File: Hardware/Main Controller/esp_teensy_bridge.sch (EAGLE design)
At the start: 55 parts, among them IC1 BQ79600PWRQ1, Q1 SI7611DN-T1-GE3, Q2 SI7611DN-T1-GE3, Q3 SI7611DN-T1-GE3

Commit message: fixed some inconsistencies
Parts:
- removed CCB1, CCB22, CCB23, CCB4: 220 pF, capacitor-wima:C2.5/2
- removed CCB2, CCB24, CCB25, CCB3: 2.2nf, capacitor-wima:C2.5/2
- removed COMH, COML: 5566-2, con-molex:5566-2
- removed RVC1, RVC17: 1k, rcl:R-US_R0603
- removed RVC18, RVC19, RVC2, RVC3: 49, rcl:R-US_R0603
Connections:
- removed net N$6: CCB3.2, RVC3.1
- removed net N$66: CCB25.1, COMH-2.S
- removed net N$67: CCB25.2, RVC19.1
- removed net N$68: CCB24.2, RVC18.1
- removed net N$69: CCB24.1, COMH-1.S
- removed net N$7: CCB2.2, RVC2.1
- removed net N$8: CCB2.1, COML-1.S
- removed net N$9: CCB3.1, COML-2.S
- net COMHN: no longer CCB22.2, RVC17.1, RVC18.2
- net COMHP: no longer CCB23.2, RVC17.2, RVC19.2
- net COMLN: no longer CCB4.2, RVC1.2, RVC3.2
- net COMLP: no longer CCB1.2, RVC1.1, RVC2.2
- net GND: no longer CCB1.1, CCB22.1, CCB23.1, CCB4.1
- net VCC: now also CONTACTOR_N-1.S, CONTACTOR_P-1.S, CONTACTOR_PRECHARGE-1.S

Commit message: 12/1/2021
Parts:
- added COOLANT-1: 5566-2, con-molex:5566-2
- added Q4: SI7611DN-T1-GE3, SI7611DN-T1-GE3:SI7611DN-T1-GE3
- added R1: 10k, rcl:R-US_R0603
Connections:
- new net COOLANT_CTRL: Q4.G, R1.2
- new net N$6: COOLANT-1-2.S, Q4.S
- net GND: now also Q4.D, R1.1
- net VCC: now also COOLANT-1-1.S
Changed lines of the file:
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@@
 <part name="R7" library="rcl" library_urn="urn:adsk.eagle:library:334" deviceset="R-US_" device="R0603" package3d_urn="urn:adsk.eagle:package:23555/3" value="10k"/>
 <part name="R8" library="rcl" library_urn="urn:adsk.eagle:library:334" deviceset="R-US_" device="R0603" package3d_urn="urn:adsk.eagle:package:23555/3" value="100k"/>
+<part name="COOLANT-1" library="con-molex" library_urn="urn:adsk.eagle:library:165" deviceset="5566-2" device="" package3d_urn="urn:adsk.eagle:package:8078583/1"/>
+<part name="Q4" library="SI7611DN-T1-GE3" deviceset="SI7611DN-T1-GE3" device=""/>
+<part name="R1" library="rcl" library_urn="urn:adsk.eagle:library:334" deviceset="R-US_" device="R0603" package3d_urn="urn:adsk.eagle:package:23555/3" value="10k"/>
 </parts>
 <sheets>
@@
 <attribute name="NAME" x="-13.97" y="67.5386" size="1.778" layer="95"/>
 <attribute name="VALUE" x="-13.97" y="62.738" size="1.778" layer="96"/>
+</instance>
+<instance part="COOLANT-1" gate="-1" x="-119.38" y="12.7" smashed="yes">
+<attribute name="NAME" x="-116.84" y="11.938" size="1.524" layer="95"/>
+<attribute name="VALUE" x="-120.142" y="14.097" size="1.778" layer="96"/>
+</instance>
+<instance part="COOLANT-1" gate="-2" x="-119.38" y="7.62" smashed="yes">
+<attribute name="NAME" x="-116.84" y="6.858" size="1.524" layer="95"/>
+<attribute name="VALUE" x="-120.142" y="9.017" size="1.778" layer="96"/>
+</instance>
+<instance part="Q4" gate="G$1" x="-132.08" y="10.16" smashed="yes">
+<attribute name="VALUE" x="-140.97796875" y="3.804309375" size="1.779590625" layer="96"/>
+<attribute name="NAME" x="-140.987490625" y="13.977490625" size="1.7815" layer="95"/>
+</instance>
+<instance part="R1" gate="G$1" x="-139.7" y="17.78" smashed="yes">
+<attribute name="NAME" x="-143.51" y="19.2786" size="1.778" layer="95"/>
+<attribute name="VALUE" x="-143.51" y="14.478" size="1.778" layer="96"/>
 </instance>
 </instances>
@@
 <label x="-15.24" y="-50.8" size="1.778" layer="95"/>
 </segment>
+<segment>
+<pinref part="Q4" gate="G$1" pin="D"/>
+<wire x1="-129.54" y1="5.08" x2="-129.54" y2="2.54" width="0.1524" layer="91"/>
+<label x="-129.54" y="0" size="1.778" layer="95"/>
+<wire x1="-144.78" y1="17.78" x2="-144.78" y2="2.54" width="0.1524" layer="91"/>
+<wire x1="-144.78" y1="2.54" x2="-129.54" y2="2.54" width="0.1524" layer="91"/>
+<pinref part="R1" gate="G$1" pin="1"/>
+</segment>
 </net>
 <net name="NCS/CS" class="0">
@@
 <wire x1="-121.92" y1="35.56" x2="-124.46" y2="35.56" width="0.1524" layer="91"/>
 <label x="-124.46" y="35.56" size="1.778" layer="95"/>
+</segment>
+<segment>
+<pinref part="COOLANT-1" gate="-1" pin="S"/>
+<wire x1="-121.92" y1="12.7" x2="-124.46" y2="12.7" width="0.1524" layer="91"/>
+<label x="-124.46" y="12.7" size="1.778" layer="95"/>
 </segment>
 </net>
@@
 </segment>
 </net>
+<net name="N$6" class="0">
+<segment>
+<pinref part="Q4" gate="G$1" pin="S"/>
+<wire x1="-129.54" y1="15.24" x2="-127" y2="15.24" width="0.1524" layer="91"/>
+<wire x1="-127" y1="15.24" x2="-127" y2="7.62" width="0.1524" layer="91"/>
+<pinref part="COOLANT-1" gate="-2" pin="S"/>
+<wire x1="-127" y1="7.62" x2="-121.92" y2="7.62" width="0.1524" layer="91"/>
+</segment>
+</net>
+<net name="COOLANT_CTRL" class="0">
+<segment>
+<pinref part="Q4" gate="G$1" pin="G"/>
+<wire x1="-134.62" y1="17.78" x2="-134.62" y2="12.7" width="0.1524" layer="91"/>
+<label x="-132.08" y="17.78" size="1.778" layer="95"/>
+<pinref part="R1" gate="G$1" pin="2"/>
+</segment>
+</net>

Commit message: have fun with eagle
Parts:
- C1, C2, C4, C5: device capacitor-wima:C2,5-3 -> rcl:C-EUC0603
- C3: device capacitor-wima:C2.5/2 -> rcl:C-EUC0603
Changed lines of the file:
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@@
 <part name="IC1" library="BQ79600" deviceset="BQ79600PWRQ1" device=""/>
 <part name="U$2" library="ESP32-DEVKITV1" deviceset="ESP32DEVKITV1" device=""/>
-<part name="C1" library="capacitor-wima" library_urn="urn:adsk.eagle:library:116" deviceset="C" device="2,5-3" package3d_urn="urn:adsk.eagle:package:5436/1" value="0.22μF"/>
-<part name="C2" library="capacitor-wima" library_urn="urn:adsk.eagle:library:116" deviceset="C" device="2,5-3" package3d_urn="urn:adsk.eagle:package:5436/1" value="0.1μF"/>
-<part name="C3" library="capacitor-wima" library_urn="urn:adsk.eagle:library:116" deviceset="C" device="2.5/2" package3d_urn="urn:adsk.eagle:package:5415/1" value="0.22uF"/>
+<part name="C1" library="rcl" library_urn="urn:adsk.eagle:library:334" deviceset="C-EU" device="C0603" package3d_urn="urn:adsk.eagle:package:23616/2" value="0.22μF"/>
+<part name="C2" library="rcl" library_urn="urn:adsk.eagle:library:334" deviceset="C-EU" device="C0603" package3d_urn="urn:adsk.eagle:package:23616/2" value="0.1μF"/>
+<part name="C3" library="rcl" library_urn="urn:adsk.eagle:library:334" deviceset="C-EU" device="C0603" package3d_urn="urn:adsk.eagle:package:23616/2" value="0.22uF"/>
 <part name="TME1205S" library="dc-dc-converter" library_urn="urn:adsk.eagle:library:208" deviceset="NME" device="" package3d_urn="urn:adsk.eagle:package:12313/1"/>
 <part name="GND1" library="supply1" library_urn="urn:adsk.eagle:library:371" deviceset="GND" device=""/>
-<part name="C5" library="capacitor-wima" library_urn="urn:adsk.eagle:library:116" deviceset="C" device="2,5-3" package3d_urn="urn:adsk.eagle:package:5436/1" value="0.22μF"/>
+<part name="C5" library="rcl" library_urn="urn:adsk.eagle:library:334" deviceset="C-EU" device="C0603" package3d_urn="urn:adsk.eagle:package:23616/2" value="0.22μF"/>
 <part name="P+1" library="supply1" library_urn="urn:adsk.eagle:library:371" deviceset="VCC" device="" value="12v"/>
-<part name="C4" library="capacitor-wima" library_urn="urn:adsk.eagle:library:116" deviceset="C" device="2,5-3" package3d_urn="urn:adsk.eagle:package:5436/1" value="0.1μF"/>
+<part name="C4" library="rcl" library_urn="urn:adsk.eagle:library:334" deviceset="C-EU" device="C0603" package3d_urn="urn:adsk.eagle:package:23616/2" value="0.1μF"/>
 <part name="CAN" library="con-molex" library_urn="urn:adsk.eagle:library:165" deviceset="5566-4" device="" package3d_urn="urn:adsk.eagle:package:8078582/1"/>
 <part name="PWR_IN" library="con-molex" library_urn="urn:adsk.eagle:library:165" deviceset="5566-2" device="" package3d_urn="urn:adsk.eagle:package:8078583/1"/>

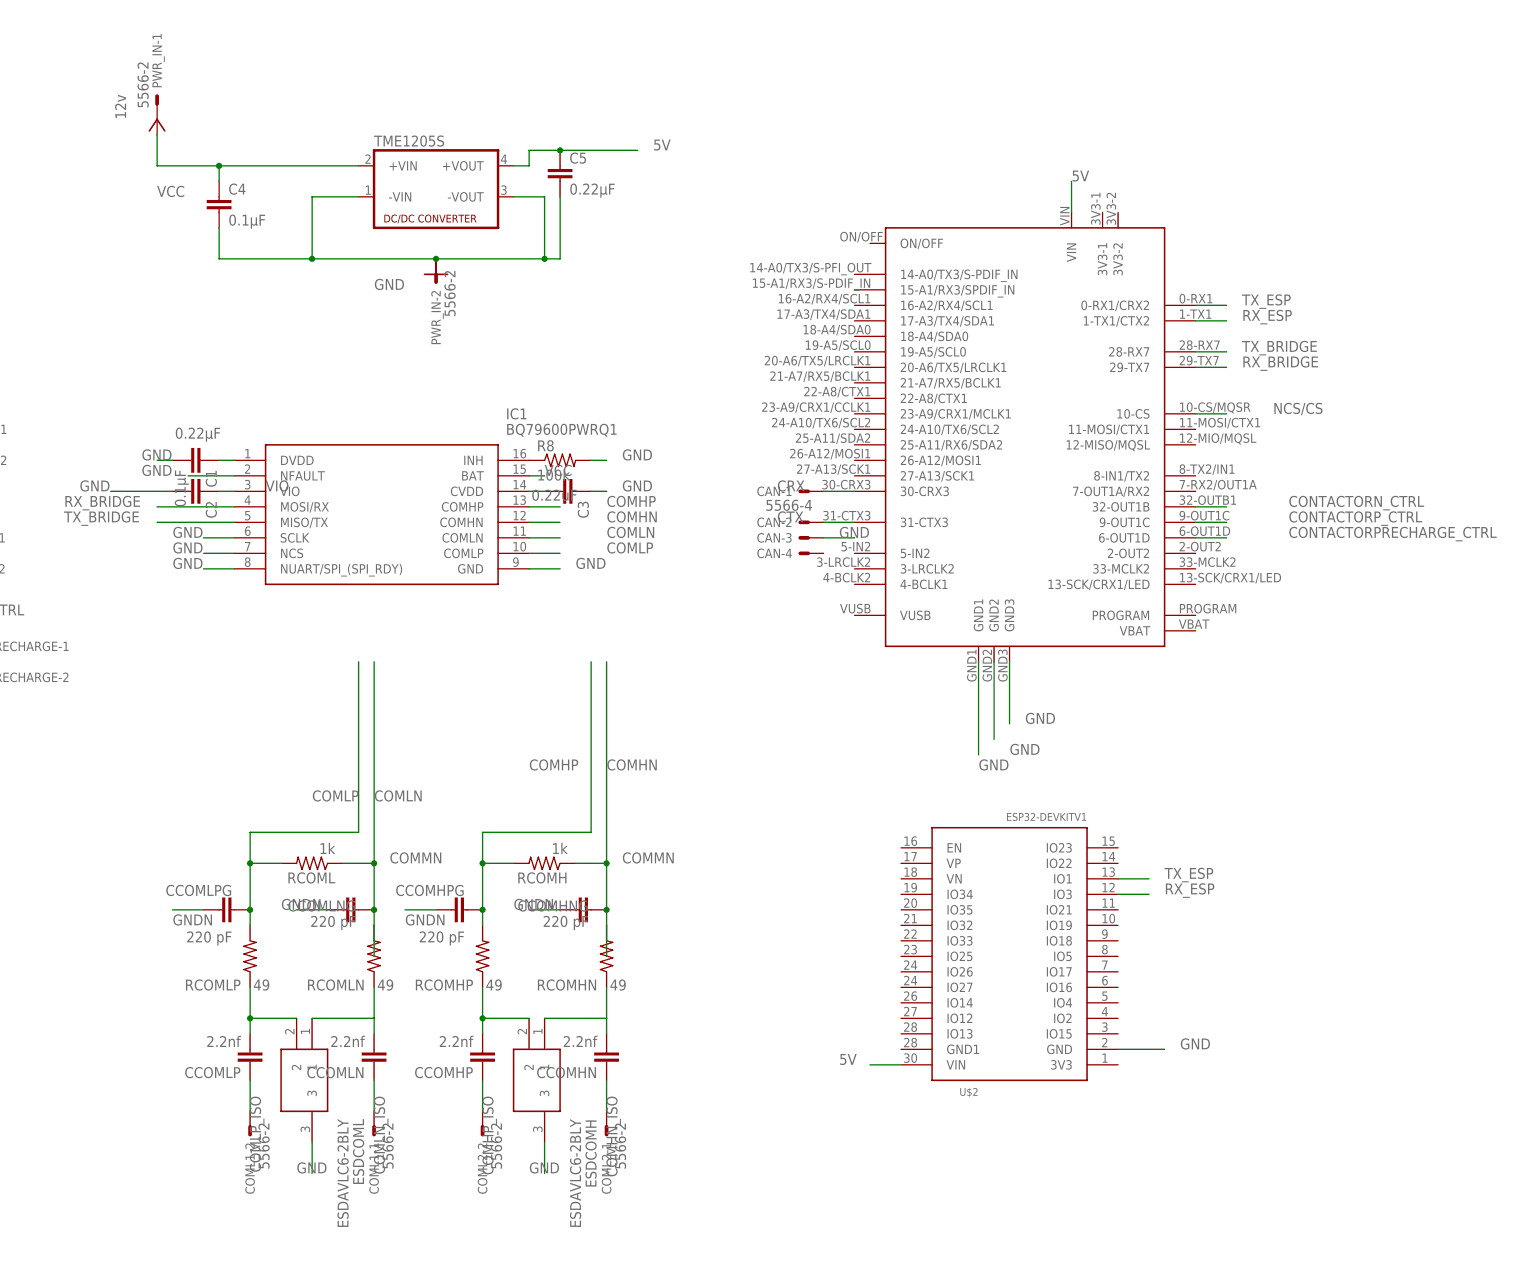
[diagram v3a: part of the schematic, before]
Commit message: changed the Teensy chip
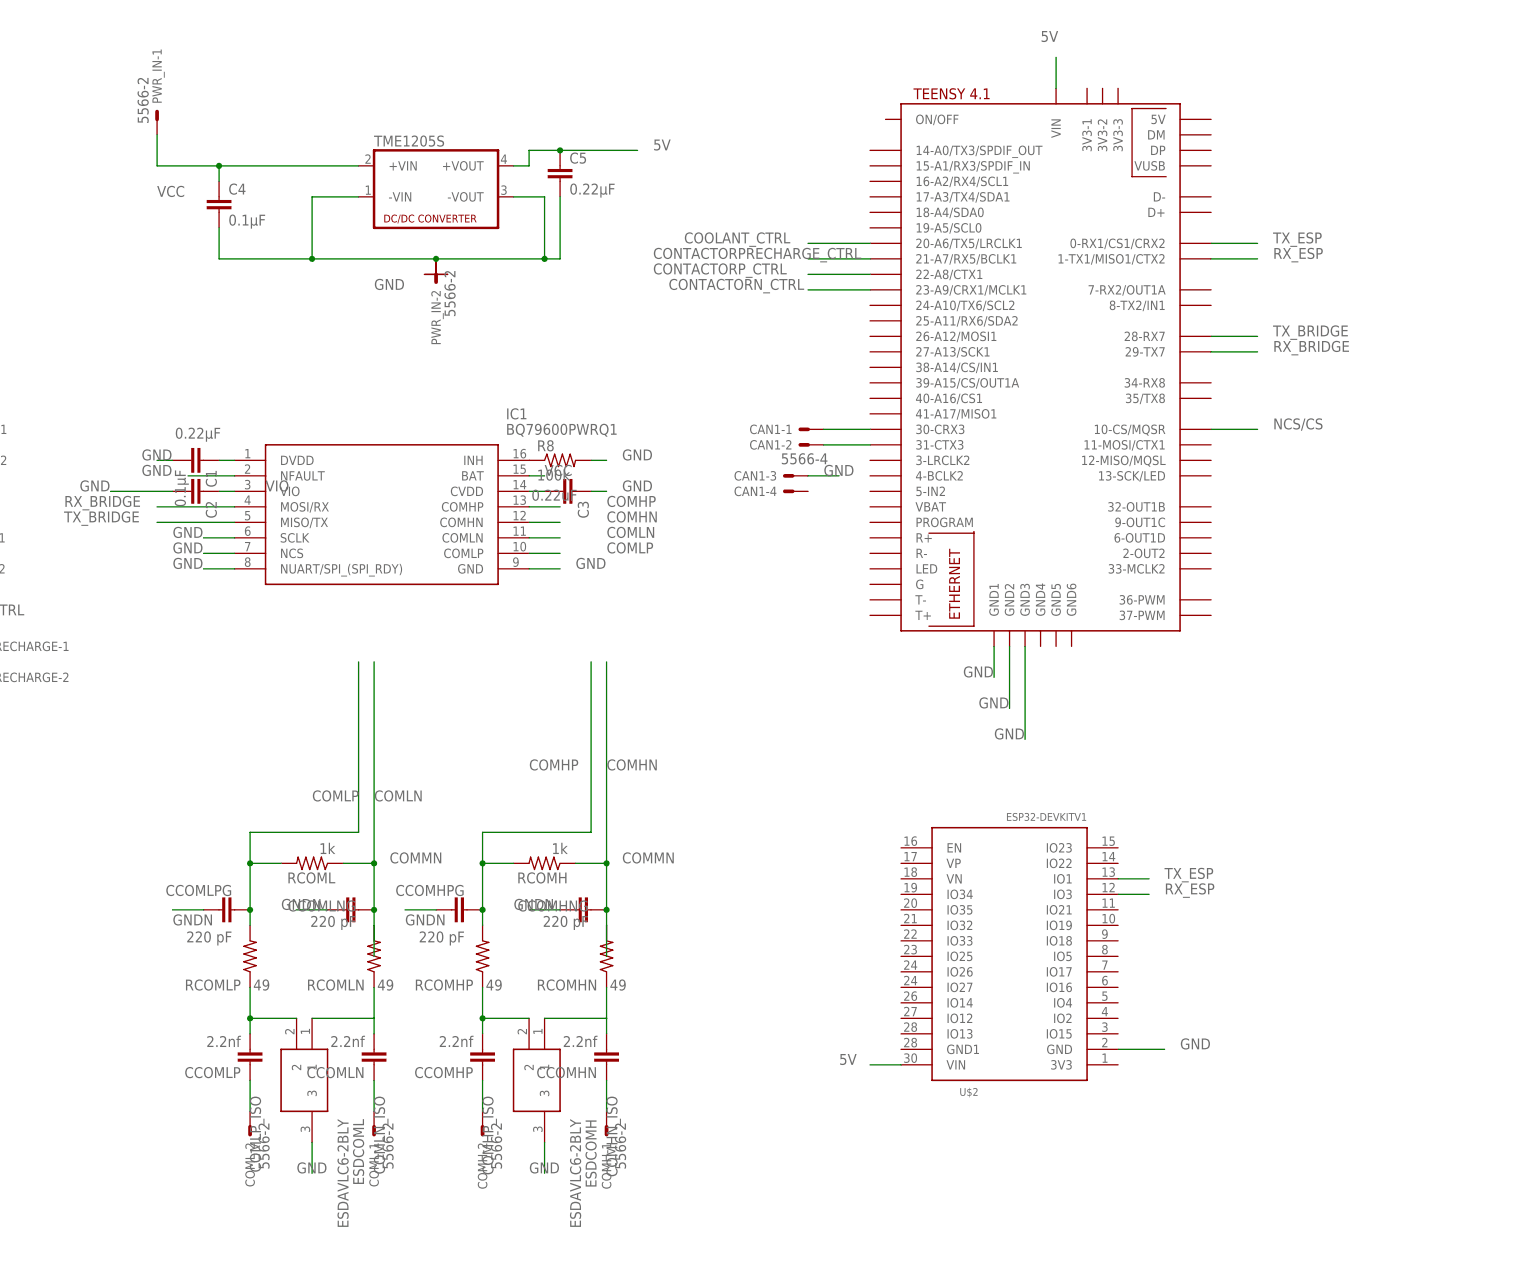
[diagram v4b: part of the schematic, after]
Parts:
- removed CAN: 5566-4, con-molex:5566-4
- removed U$1: TEENSY40, teensy:TEENSY40
- added CAN1: 5566-4, con-molex:5566-4
- added U$3: TEENSY41, teensy:TEENSY41
- renumbered COML1 to COML, COML2 to COMH
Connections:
- removed net CRX: CAN-1.S, U$1.30-CRX3
- removed net CTX: CAN-2.S, U$1.31-CTX3
- new net N$7: CAN1-1.S, U$3.30-CRX3
- new net N$8: CAN1-2.S, U$3.31-CTX3
- net 5V: now also U$3.VIN; no longer U$1.VIN
- net CONTACTORN_CTRL: now also U$3.23-A9/CRX1/MCLK1; no longer U$1.32-OUT1B
- net CONTACTORPRECHARGE_CTRL: now also U$3.21-A7/RX5/BCLK1; no longer U$1.6-OUT1D
- net CONTACTORP_CTRL: now also U$3.22-A8/CTX1; no longer U$1.9-OUT1C
- net COOLANT_CTRL: now also U$3.20-A6/TX5/LRCLK1
- net GND: now also CAN1-3.S, U$3.GND1, U$3.GND2, U$3.GND3; no longer CAN-3.S, U$1.GND1, U$1.GND2, U$1.GND3
- net NCS/CS: now also U$3.10-CS/MQSR; no longer U$1.10-CS
- net RX_BRIDGE: now also U$3.29-TX7; no longer U$1.29-TX7
- net RX_ESP: now also U$3.1-TX1/MISO1/CTX2; no longer U$1.1-TX1/CTX2
- net TX_BRIDGE: now also U$3.28-RX7; no longer U$1.28-RX7
- net TX_ESP: now also U$3.0-RX1/CS1/CRX2; no longer U$1.0-RX1/CRX2
- net VCC: now also PWR_IN-1.S
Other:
- moved on the sheet: PWR_IN-1
